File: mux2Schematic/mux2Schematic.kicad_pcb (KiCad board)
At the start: 2 copper layers, 215 x 58 mm, 64 parts, among them J1 Conn_02x12_Odd_Even, J10 Conn_02x06_Top_Bottom, J11 Conn_02x06_Top_Bottom, J12 Conn_02x06_Top_Bottom, J13 Conn_02x06_Top_Bottom, J14 Conn_02x06_Top_Bottom, J15 Conn_01x02, J16 Conn_01x02, J17 Conn_01x02, J18 Conn_01x02, J19 Conn_01x02, J2 Conn_02x06_Top_Bottom, J20 Conn_01x02, J21 Conn_01x02, J3 Banana, J30 Conn_01x8, J31 Conn_01x8, J32 Conn_01x02, J33 Conn_01x02, J34 Conn_01x02, J35 Conn_01x02, J36 Conn_01x02, J37 Conn_01x02, J38 Conn_01x02, J39 Conn_01x02, J4 Banana, J5 Conn_01x8, J6 Conn_01x02, J7 Conn_02x06_Top_Bottom, J8 Conn_01x10, J9 Conn_02x06_Top_Bottom, U1 CD74HC4051E, U2 AMS1117-1.8, U3 AZ1084-3.3

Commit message: a few edits to PCB P1
based on design review. still need to route traces
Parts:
- moved J4 1.20 mm to (124.5, 135.2)
- moved J3 1.20 mm to (107.8, 135.2)
- moved C1 0.66 mm to (183.5, 137.2)
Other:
- board text added: "CS0 CS2 CS4 CS6"
- board text added: "CS1 CS3 CS5 CS7"
- board text added: "OG0 OG1 OG2 OG3"
- board text added: "OG4 OG5 OG6 OG7"
- board text added: "S0 S2 COPI ~{LDAC} ~{CLR}"
- board text added: "S1 SCLK CS ~{RESET} GND"
- board text added: "VO0 VO1 VO2 VO3"
- board text added: "VO4 VO5 VO6 VO7"
- board text added: "add 1x6 IDC connector for VCC"
- board text added: "add another IDC on DAC out for P2"
- board text added: "add silkscree"
- board text added: "add silkscreen"
- board text added: "and LEDs"
- board text added: "split into two PCBs"
- board text removed: "Is this gap wide enough?"

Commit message: minor tweaks to PCB
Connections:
- J1 pad 10: unconnected-(J1-Pin_10-Pad10) -> /~{LDAC}
- J1 pad 12: unconnected-(J1-Pin_12-Pad12) -> /SCLK
- J1 pad 16: unconnected-(J1-Pin_16-Pad16) -> /CIPO
- J1 pad 18: unconnected-(J1-Pin_18-Pad18) -> /COPI
- J1 pad 19: unconnected-(J1-Pin_19-Pad19) -> /CS
- J1 pad 21: unconnected-(J1-Pin_21-Pad21) -> /S2
- J1 pad 22: unconnected-(J1-Pin_22-Pad22) -> /S0
- J1 pad 24: unconnected-(J1-Pin_24-Pad24) -> /S1
- J1 pad 4: unconnected-(J1-Pin_4-Pad4) -> /~{CLR}
- J1 pad 6: unconnected-(J1-Pin_6-Pad6) -> /~{RESET}

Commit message: PCB finished!
Haven't thoroughly looked it over yet
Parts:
- added D1: HSMA-C170, LED_SMD:LED_0805_2012Metric, F.Cu at (116.4, 146.7)
- added D10: HSMA-C170, LED_SMD:LED_0805_2012Metric, F.Cu at (239.5, 142.9)
- added D11: HSMA-C170, LED_SMD:LED_0805_2012Metric, F.Cu at (237.0, 142.9)
- added D12: HSMA-C170, LED_SMD:LED_0805_2012Metric, F.Cu at (229.4, 142.9)
- added D13: HSMA-C170, LED_SMD:LED_0805_2012Metric, F.Cu at (234.5, 142.9)
- added D14: HSMA-C170, LED_SMD:LED_0805_2012Metric, F.Cu at (226.8, 142.9)
- added D15: HSMA-C170, LED_SMD:LED_0805_2012Metric, F.Cu at (231.9, 142.9)
- added D16: HSMA-C170, LED_SMD:LED_0805_2012Metric, F.Cu at (224.3, 142.9)
- added D17: HSMA-C170, LED_SMD:LED_0805_2012Metric, F.Cu at (221.7, 142.9)
- added D18: HSMA-C170, LED_SMD:LED_0805_2012Metric, F.Cu at (244.6, 142.9)
- added D19: HSMA-C170, LED_SMD:LED_0805_2012Metric, F.Cu at (242.1, 142.9)
- added D2: HSMA-C170, LED_SMD:LED_0805_2012Metric, F.Cu at (210.7, 142.8)
- added D3: HSMA-C170, LED_SMD:LED_0805_2012Metric, F.Cu at (205.6, 142.8)
- added D4: HSMA-C170, LED_SMD:LED_0805_2012Metric, F.Cu at (208.2, 142.8)
- added D5: HSMA-C170, LED_SMD:LED_0805_2012Metric, F.Cu at (195.5, 142.8)
- added D6: HSMA-C170, LED_SMD:LED_0805_2012Metric, F.Cu at (192.9, 142.8)
- added D7: HSMA-C170, LED_SMD:LED_0805_2012Metric, F.Cu at (203.1, 142.8)
- added D8: HSMA-C170, LED_SMD:LED_0805_2012Metric, F.Cu at (200.5, 142.8)
- added D9: HSMA-C170, LED_SMD:LED_0805_2012Metric, F.Cu at (198.0, 142.8)
- added JP2: SolderJumper_2_Bridged, Jumper:SolderJumper-2_P1.3mm_Bridged_RoundedPad1.0x1.5mm, F.Cu at (216.4, 137.8)
- added R1: 5.1k, Resistor_SMD:R_0805_2012Metric, F.Cu at (116.4, 143.3)
- added R10: 2.2k, Resistor_SMD:R_0805_2012Metric, F.Cu at (208.2, 139.3)
- added R11: 2.2k, Resistor_SMD:R_0805_2012Metric, F.Cu at (200.5, 139.3)
- added R12: 2.2k, Resistor_SMD:R_0805_2012Metric, F.Cu at (192.9, 139.3)
- added R13: 2.2k, Resistor_SMD:R_0805_2012Metric, F.Cu at (203.1, 139.3)
- added R14: 2.2k, Resistor_SMD:R_0805_2012Metric, F.Cu at (205.6, 139.3)
- added R15: 2.2k, Resistor_SMD:R_0805_2012Metric, F.Cu at (210.7, 139.3)
- added R16: 2.2k, Resistor_SMD:R_0805_2012Metric, F.Cu at (198.0, 139.3)
- added R17: 2.2k, Resistor_SMD:R_0805_2012Metric, F.Cu at (195.5, 139.3)
- added R18: 2.2k, Resistor_SMD:R_0805_2012Metric, F.Cu at (221.7, 139.4)
- added R19: 2.2k, Resistor_SMD:R_0805_2012Metric, F.Cu at (237.0, 139.4)
- added R20: 2.2k, Resistor_SMD:R_0805_2012Metric, F.Cu at (231.9, 139.4)
- added R21: 2.2k, Resistor_SMD:R_0805_2012Metric, F.Cu at (224.3, 139.4)
- added R22: 2.2k, Resistor_SMD:R_0805_2012Metric, F.Cu at (234.4, 139.4)
- added R23: 2.2k, Resistor_SMD:R_0805_2012Metric, F.Cu at (229.4, 139.4)
- added R24: 2.2k, Resistor_SMD:R_0805_2012Metric, F.Cu at (239.5, 139.4)
- added R25: 2.2k, Resistor_SMD:R_0805_2012Metric, F.Cu at (226.8, 139.4)
- added R26: 2.2k, Resistor_SMD:R_0805_2012Metric, F.Cu at (242.1, 139.4)
- added R27: 2.2k, Resistor_SMD:R_0805_2012Metric, F.Cu at (244.6, 139.4)
- R2: renamed from R7; value 10k -> 5.1k
- R3: renamed from R2; value 10k -> 5.1k
- R4: value 10k -> 5.1k
- R5: renamed from R3; value 10k -> 5.1k
- R6: renamed from R1; value 10k -> 5.1k
- R7: renamed from R5; value 10k -> 5.1k
- R8: renamed from R6; value 10k -> 5.1k
- R9: renamed from R8; value 10k -> 5.1k
- moved J10 23.9 mm to (124.2, 124.3)
- moved J8 23.9 mm to (100.2, 124.3)
- moved U3 12.0 mm to (175.1, 150.0)
- moved JP1 11.8 mm to (166.4, 150.3)
- moved R6 11.7 mm to (182.5, 142.8)
- moved J1 11.6 mm to (63.2, 149.3)
- moved H1 11.6 mm to (54.0, 149.0)
- moved H2 11.5 mm to (254.0, 149.0)
- moved R3 11.3 mm to (180.3, 142.8)
- moved R5 10.9 mm to (178.2, 142.8)
- moved C5 10.8 mm to (180.7, 147.7), turned to 0 degrees
- moved R4 10.6 mm to (176.1, 142.8)
- moved R7 10.3 mm to (174.0, 142.8)
- moved R8 10.1 mm to (171.8, 142.8)
- moved J2 10.0 mm to (107.8, 145.2)
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- renumbered C3 to C1, C4 to C3, C5 to C4, C1 to C5, H2 to H1, H4 to H2, H1 to H3, H3 to H4, J13 to J10, J34 to J11, J35 to J12, J11 to J13, J36 to J14, J10 to J15, J37 to J16, J9 to J17, J7 to J18, J38 to J19, J3 to J2, J39 to J20, J2 to J21, J6 to J22, J22 to J23, J15 to J24, J5 to J25, J23 to J26, J16 to J27, J24 to J28, J25 to J29, J4 to J3, J17 to J30, J26 to J31, J18 to J32, J27 to J33, J19 to J34, J31 to J35, J20 to J36, J28 to J37, J29 to J38, J21 to J39, J30 to J4, J8 to J5, J32 to J6, J14 to J7, J12 to J8, J33 to J9, JP3 to JP1, U3 to U1, U1 to U3
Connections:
- J1 pad 10: /~{LDAC} -> /CIPO
- J1 pad 12: /SCLK -> /~{RESET}
- J1 pad 16: /CIPO -> /SCLK
- J1 pad 6: /~{RESET} -> /~{LDAC}
- J5 pad 10: GND -> /~{CLR}
- J5 pad 4: /SCLK -> /CS
- J5 pad 6: /CS -> /SCLK
- J5 pad 7: /~{LDAC} -> /CIPO
- J5 pad 8: /~{RESET} -> /~{LDAC}
- J5 pad 9: /~{CLR} -> /~{RESET}
- U3 pad 13: /CS_0 -> /CS_2
- U3 pad 15: /CS_2 -> /CS_0
- U3 pad 2: /CS_6 -> /CS_5
- U3 pad 4: /CS_7 -> /CS_6
- U3 pad 5: /CS_5 -> /CS_7
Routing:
- net /COPI: track 0.00 -> 315.2 mm, vias 0 -> 7
- net /SCLK: track 0.00 -> 298.4 mm, vias 0 -> 9
- net /~{RESET}: track 0.00 -> 281.7 mm, vias 0 -> 9
- net /IOVcc: track 0.00 -> 279.4 mm, vias 0 -> 9
- net /CIPO: track 0.00 -> 263.0 mm, vias 0 -> 8
- net /VCC: track 0.00 -> 247.3 mm, vias 0 -> 14
- net /~{LDAC}: track 0.00 -> 242.0 mm, vias 0 -> 1
- net /~{CLR}: track 0.00 -> 239.0 mm, vias 0 -> 1
- net /CS: track 0.00 -> 189.3 mm, vias 0 -> 3
- net /CS_7: track 0.00 -> 165.1 mm, vias 0 -> 1
- net /S2: track 0.00 -> 149.1 mm, vias 0 -> 4
- net /S0: track 0.00 -> 146.4 mm, vias 0 -> 4
- net /S1: track 0.00 -> 142.9 mm, vias 0 -> 4
- net /CS_6: track 0.00 -> 137.4 mm, vias 0 -> 1
- net /CS_5: track 0.00 -> 112.2 mm, vias 0 -> 1
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- added copper zone on B.Cu, net GND
- added copper zone on F.Cu, net GND
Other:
- board size 215 x 58 mm -> 214 x 70 mm
- board text added: "S0 S2 ~{CLR} ~{LDAC} SCLK"
- board text added: "S1 CS ~{RESET} CIPO COPI"
- board text added: "add an IDC for DAC out for Prototype 2"
- board text removed: "Are there any signals sensitive to parasitic inductance from vias?"
- board text removed: "S0 S2 COPI ~{LDAC} ~{CLR}"
- board text removed: "S1 SCLK CS ~{RESET} GND"
- board text removed: "add another IDC on DAC out for P2"
- board text removed: "add silkscree"
- board text removed: "add silkscreen"
- board text removed: "and LEDs"
- board text removed: "is this plated hole footprint for the bananas good?"
- board text removed: "split into two PCBs"

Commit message: nvm it's not done
fixed most of the problem
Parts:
- J10, J13, J15, J17, J18, J21, J7, J8: value Conn_02x06_Top_Bottom -> Conn_02x06_Odd_Even
- moved J13 7.39 mm to (140.7, 124.0)
- moved D5 7.39 mm to (188.1, 142.5)
- moved D9 7.39 mm to (190.6, 142.5)
- moved J32 7.39 mm to (165.9, 108.1)
- moved J37 7.39 mm to (213.9, 98.4)
- moved R16 7.39 mm to (190.6, 139.1)
- moved R17 7.39 mm to (188.1, 139.1)
- moved R5 7.39 mm to (170.8, 142.5)
- moved J10 7.39 mm to (116.8, 124.0)
- moved J25 7.39 mm to (97.3, 90.0)
- moved J27 7.39 mm to (118.0, 108.1)
- moved J9 7.39 mm to (97.8, 122.0)
- moved H1 7.39 mm to (46.6, 148.7)
- moved H3 7.39 mm to (46.6, 118.7)
- moved H5 7.39 mm to (46.6, 92.7)
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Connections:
- J1 pad 10: /CIPO -> /~{CLR}
- J1 pad 12: /~{RESET} -> /COPI
- J1 pad 16: /SCLK -> /CIPO
- J1 pad 18: /COPI -> /SCLK
- J1 pad 4: /~{CLR} -> /~{LDAC}
- J1 pad 6: /~{LDAC} -> /~{RESET}
- J10 pad 1: /CS_5 -> /IOVcc
- J10 pad 10: unconnected-(J13-Pin_10-Pad10) -> /~{RESET}
- J10 pad 11: GND -> /CS_5
- J10 pad 12: /IOVcc -> /~{LDAC}
- J10 pad 2: /COPI -> /IOVcc
- J10 pad 3: /CIPO -> GND
- J10 pad 4: /SCLK -> GND
- J10 pad 5: GND -> /SCLK
- J10 pad 6: /IOVcc -> unconnected-(J10-Pin_6-Pad6)
- J10 pad 7: /~{LDAC} -> /CIPO
- J10 pad 8: /~{RESET} -> /~{CLR}
- J10 pad 9: /~{CLR} -> /COPI
- J13 pad 1: /CS_4 -> /IOVcc
- J13 pad 10: unconnected-(J11-Pin_10-Pad10) -> /~{RESET}
- J13 pad 11: GND -> /CS_4
- J13 pad 12: /IOVcc -> /~{LDAC}
- J13 pad 2: /COPI -> /IOVcc
- J13 pad 3: /CIPO -> GND
- J13 pad 4: /SCLK -> GND
- J13 pad 5: GND -> /SCLK
- J13 pad 6: /IOVcc -> unconnected-(J13-Pin_6-Pad6)
- J13 pad 7: /~{LDAC} -> /CIPO
- J13 pad 8: /~{RESET} -> /~{CLR}
- J13 pad 9: /~{CLR} -> /COPI
- J15 pad 1: /CS_3 -> /IOVcc
- J15 pad 10: unconnected-(J10-Pin_10-Pad10) -> /~{RESET}
- J15 pad 11: GND -> /CS_3
- J15 pad 12: /IOVcc -> /~{LDAC}
- J15 pad 2: /COPI -> /IOVcc
- J15 pad 3: /CIPO -> GND
- J15 pad 4: /SCLK -> GND
- J15 pad 5: GND -> /SCLK
- J15 pad 6: /IOVcc -> unconnected-(J15-Pin_6-Pad6)
- J15 pad 7: /~{LDAC} -> /CIPO
- J15 pad 8: /~{RESET} -> /~{CLR}
- J15 pad 9: /~{CLR} -> /COPI
- J17 pad 1: /CS_2 -> /IOVcc
- J17 pad 10: unconnected-(J9-Pin_10-Pad10) -> /~{RESET}
- J17 pad 11: GND -> /CS_2
- J17 pad 12: /IOVcc -> /~{LDAC}
- J17 pad 2: /COPI -> /IOVcc
- J17 pad 3: /CIPO -> GND
- J17 pad 4: /SCLK -> GND
- J17 pad 5: GND -> /SCLK
- J17 pad 6: /IOVcc -> unconnected-(J17-Pin_6-Pad6)
- J17 pad 7: /~{LDAC} -> /CIPO
- J17 pad 8: /~{RESET} -> /~{CLR}
- J17 pad 9: /~{CLR} -> /COPI
- J18 pad 1: /CS_1 -> /IOVcc
- J18 pad 10: unconnected-(J7-Pin_10-Pad10) -> /~{RESET}
- J18 pad 11: GND -> /CS_1
- J18 pad 12: /IOVcc -> /~{LDAC}
- J18 pad 2: /COPI -> /IOVcc
- J18 pad 3: /CIPO -> GND
- J18 pad 4: /SCLK -> GND
- J18 pad 5: GND -> /SCLK
- J18 pad 6: /IOVcc -> unconnected-(J18-Pin_6-Pad6)
- J18 pad 7: /~{LDAC} -> /CIPO
- J18 pad 8: /~{RESET} -> /~{CLR}
- J18 pad 9: /~{CLR} -> /COPI
- J21 pad 1: /CS_0 -> /IOVcc
- J21 pad 10: unconnected-(J2-Pin_10-Pad10) -> /~{RESET}
- J21 pad 11: GND -> /CS_0
- J21 pad 12: /IOVcc -> /~{LDAC}
- J21 pad 2: /COPI -> /IOVcc
- J21 pad 3: /CIPO -> GND
- J21 pad 4: /SCLK -> GND
- J21 pad 5: GND -> /SCLK
- J21 pad 6: /IOVcc -> unconnected-(J21-Pin_6-Pad6)
- J21 pad 7: /~{LDAC} -> /CIPO
- J21 pad 8: /~{RESET} -> /~{CLR}
- J21 pad 9: /~{CLR} -> /COPI
- J7 pad 1: /CS_7 -> /IOVcc
- J7 pad 10: unconnected-(J14-Pin_10-Pad10) -> /~{RESET}
- J7 pad 11: GND -> /CS_7
- J7 pad 12: /IOVcc -> /~{LDAC}
- J7 pad 2: /COPI -> /IOVcc
- J7 pad 3: /CIPO -> GND
- J7 pad 4: /SCLK -> GND
- J7 pad 5: GND -> /SCLK
- J7 pad 6: /IOVcc -> unconnected-(J7-Pin_6-Pad6)
- J7 pad 7: /~{LDAC} -> /CIPO
- J7 pad 8: /~{RESET} -> /~{CLR}
- J7 pad 9: /~{CLR} -> /COPI
- J8 pad 1: /CS_6 -> /IOVcc
- J8 pad 10: unconnected-(J12-Pin_10-Pad10) -> /~{RESET}
- J8 pad 11: GND -> /CS_6
- J8 pad 12: /IOVcc -> /~{LDAC}
- J8 pad 2: /COPI -> /IOVcc
- J8 pad 3: /CIPO -> GND
- J8 pad 4: /SCLK -> GND
- J8 pad 5: GND -> /SCLK
- J8 pad 6: /IOVcc -> unconnected-(J8-Pin_6-Pad6)
- J8 pad 7: /~{LDAC} -> /CIPO
- J8 pad 8: /~{RESET} -> /~{CLR}
- J8 pad 9: /~{CLR} -> /COPI
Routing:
- net /~{CLR}: track 239.0 -> 305.9 mm, vias 1 -> 2
- net /~{RESET}: track 281.7 -> 221.8 mm, vias 9 -> 0
- net /COPI: track 315.2 -> 263.9 mm, vias 7 -> 0
- net /SCLK: track 298.4 -> 271.3 mm, vias 9 -> 8
- net /VCC: track 247.3 -> 268.4 mm, vias 14 -> 10
- net /CS_4: track 87.1 -> 100.0 mm
- net /CS_5: track 112.2 -> 124.9 mm
- net /~{LDAC}: track 242.0 -> 254.5 mm
- net /CS_6: track 137.4 -> 149.8 mm
- net /CS_1: track 87.6 -> 75.2 mm
- net /CS_3: track 57.0 -> 69.2 mm
- net /CS_2: track 67.9 -> 56.1 mm
- net /IOVcc: track 279.4 -> 291.0 mm, vias 9 -> 15
- net /CS_0: track 106.1 -> 95.2 mm
- net /CS_7: track 165.1 -> 173.8 mm
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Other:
- board text added: "1x6 IDC connector for VCC would go here ->"
- board text removed: "add 1x6 IDC connector for VCC"
- board text removed: "add an IDC for DAC out for Prototype 2"

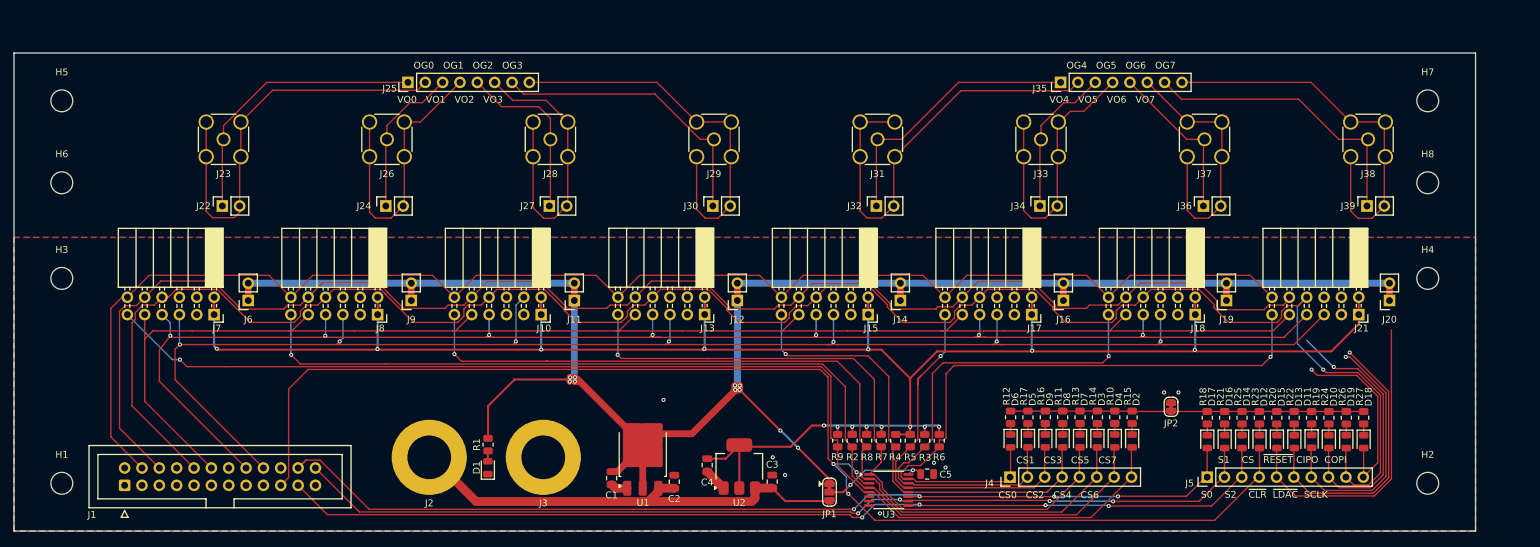
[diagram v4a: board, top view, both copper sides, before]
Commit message: PCB Finalized & Ordered!
Had to manually fix a number of things (e.g. component rotation) when I ordered it on JLCPCB. I didn't add the settings that let you rotate the part automatically into the right position.
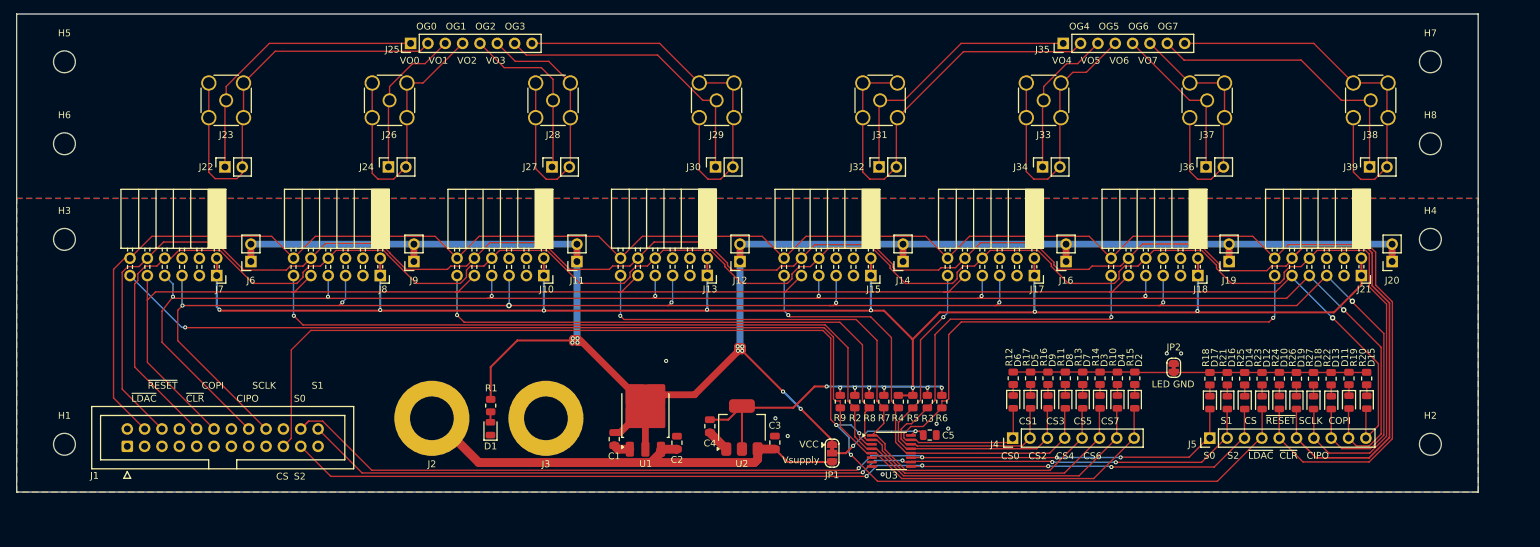
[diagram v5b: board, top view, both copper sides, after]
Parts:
- added G***: LOGO, LOGO, B.Cu at (128.8, 134.4)
- added G***: LOGO, LOGO, B.Cu at (142.4, 134.7)
- moved D15 14.4 mm to (237.7, 136.8)
- moved R20 14.4 mm to (237.7, 133.4)
- moved D18 9.31 mm to (229.9, 136.9)
- moved R27 9.31 mm to (229.9, 133.4)
- moved D19 9.27 mm to (227.4, 136.9)
- moved R26 9.27 mm to (227.4, 133.4)
- moved D10 9.24 mm to (224.9, 136.9)
- moved R24 9.24 mm to (224.9, 133.4)
- moved D11 7.94 mm to (235.1, 136.8)
- moved R19 7.94 mm to (235.1, 133.4)
- moved D13 7.87 mm to (232.5, 136.9)
- moved R22 7.87 mm to (232.5, 133.4)
- moved J37 5.73 mm to (214.3, 92.6)
- moved R16 5.73 mm to (191.0, 133.3)
- moved R17 5.73 mm to (188.5, 133.3)
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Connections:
- J5 pad 10: /~{CLR} -> /COPI
- J5 pad 5: /COPI -> /~{LDAC}
- J5 pad 6: /SCLK -> /~{RESET}
- J5 pad 7: /CIPO -> /~{CLR}
- J5 pad 8: /~{LDAC} -> /SCLK
- J5 pad 9: /~{RESET} -> /CIPO
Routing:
- net /~{RESET}: track 221.8 -> 282.5 mm
- net /~{LDAC}: track 254.5 -> 282.7 mm, vias 1 -> 0
- net /~{CLR}: track 305.9 -> 286.1 mm, vias 2 -> 0
- net /COPI: track 263.9 -> 252.4 mm, vias 0 -> 1
- net /SCLK: track 271.3 -> 266.6 mm
- net /CIPO: track 257.6 -> 256.0 mm
- net /CS_2: track 56.1 -> 54.5 mm
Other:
- board text added: "CIPO"
- board text added: "COPI"
- board text added: "CS"
- board text added: "DAC Instrumentation Board Lucas Lemos & Jackson Philion 11/9/2024"
- board text added: "LED GND"
- board text added: "S0"
- board text added: "S0 S2 ~{LDAC} ~{CLR} CIPO"
- board text added: "S1"
- board text added: "S1 CS ~{RESET} SCLK COPI"
- board text added: "S2"
- board text added: "SCLK"
- board text added: "V-Cut"
- board text added: "VCC"
- board text added: "Vsupply"
- board text added: "~{CLR}"
- board text added: "~{LDAC}"
- board text added: "~{RESET}"
- board text removed: "<- V-Cut"
- board text removed: "S0 S2 ~{CLR} ~{LDAC} SCLK"
- board text removed: "S1 CS ~{RESET} CIPO COPI"

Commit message: Separated PCB into two PCBS
Ordering as one PCB w/ V-cut was more expensive. Also fixed placement for JLCPCB orders and narrowed the mux board since it no longer needs to be 70mm wide
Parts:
- R1: value 5.1k -> 2.2k
- R2, R3, R4, R5, R6, R7, R8, R9: value 5.1k -> 10k
- U1: value AZ1084-3.3 -> AZ1084CD-3.3TRG1
- U3: value CD74HC4051E -> CD74HC4053PWR
